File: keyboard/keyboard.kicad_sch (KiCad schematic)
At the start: 117 parts, among them J1 USB_C_Receptacle_USB2.0_16P, SW1 Keyswitch, SW10 Keyswitch, SW11 Keyswitch, SW12 Keyswitch, SW13 Keyswitch, SW14 Keyswitch, SW15 Keyswitch, SW16 Keyswitch, SW17 Keyswitch, SW18 Keyswitch, SW19 Keyswitch, SW2 Keyswitch, SW20 Keyswitch, SW21 Keyswitch, SW22 Keyswitch, SW23 Keyswitch, SW24 Keyswitch, SW25 Keyswitch, SW26 Keyswitch, SW27 Keyswitch, SW29 Keyswitch, SW3 Keyswitch, SW30 Keyswitch, SW31 Keyswitch, SW32 Keyswitch, SW33 Keyswitch, SW34 Keyswitch, SW35 Keyswitch, SW36 Keyswitch, SW37 Keyswitch, SW38 Keyswitch, SW39 Keyswitch, SW4 Keyswitch, SW40 Keyswitch, SW41 Keyswitch, SW42 Keyswitch, SW43 Keyswitch, SW44 Keyswitch, SW45 Keyswitch, SW46 Keyswitch, SW47 Keyswitch, SW48 Keyswitch, SW49 SW_SPDT, SW5 Keyswitch, SW50 SW_Push, SW6 Keyswitch, SW7 Keyswitch, SW8 Keyswitch, SW9 Keyswitch, U1 USBLC6-2P6, U2 STM32F072CBU6, U3 AP2112K-3.3

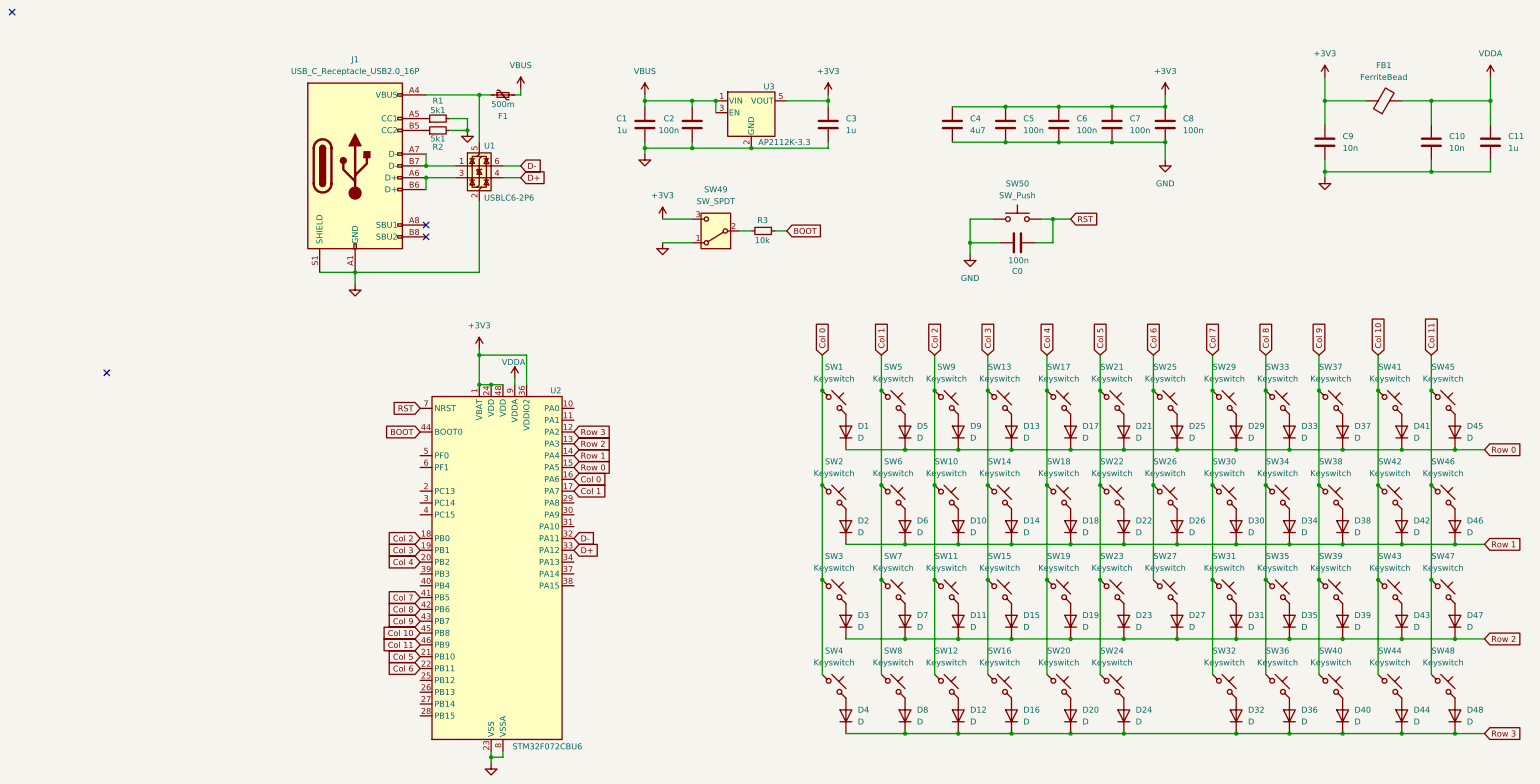
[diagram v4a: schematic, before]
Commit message: feat(keyboard): changed from QFP48 to LQFP48
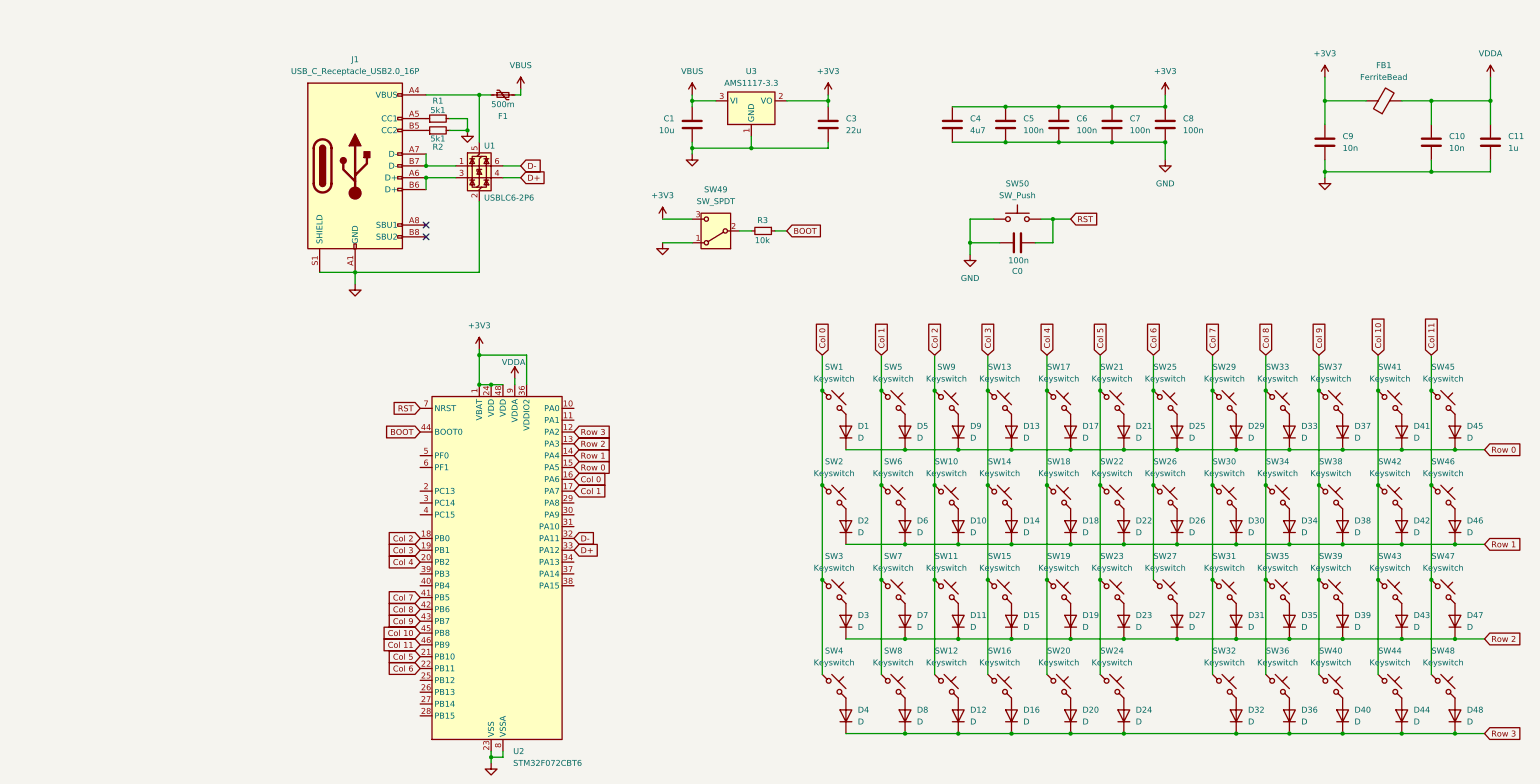
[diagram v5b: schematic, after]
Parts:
- removed C2: 100n, Capacitor_SMD:C_0603_1608Metric, symbol Device:C
- removed U2: STM32F072CBU6, Package_DFN_QFN:QFN-48-1EP_7x7mm_P0.5mm_EP5.6x5.6mm, symbol MCU_ST_STM32F0:STM32F072CBUx
- removed U3: AP2112K-3.3, Package_TO_SOT_SMD:SOT-23-5, symbol Regulator_Linear:AP2112K-3.3
- added U2: STM32F072CBT6, Package_QFP:LQFP-48_7x7mm_P0.5mm, symbol MCU_ST_STM32F0:STM32F072CBTx
- added U3: AMS1117-3.3, Package_TO_SOT_SMD:SOT-223-3_TabPin2, symbol Regulator_Linear:AMS1117-3.3
- C0, C5, C6, C7, C8: LCSC C2909627 -> C14663
- C1: value 1u -> 10u; LCSC C2691405 -> C19702
- C10, C9: LCSC C185599 -> C57112
- C11: LCSC C2691405 -> C15849
- C3: value 1u -> 22u; LCSC C2691405 -> C59461
- C4: LCSC C2918512 -> C19666
- D1, D10, D11, D12, D13, D14, D15, D16, D17, D18, D19, D2, D20, D21, D22, D23, D24, D25, D26, D27, D29, D3, D30, D31, D32, D33, D34, D35, D36, D37, D38, D39, D4, D40, D41, D42, D43, D44, D45, D46, D47, D48, D5, D6, D7, D8, D9: LCSC C402213 -> C81598
- F1: LCSC C3760867 -> C7472536
- FB1: LCSC C491555 -> C1002
- J1: LCSC C319148 -> C2686968
- R1, R2: LCSC C543856 -> C23186
- R3: LCSC C328335 -> C25804
- SW50: LCSC C202424 -> C127478
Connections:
- net +3V3: now also U2.1 (VBAT), U2.24 (VDD), U2.36 (VDDIO2), U2.48 (VDD), U3.2 (VO)
- net BOOT: now also U2.44 (BOOT0)
- net Col 0: now also U2.16 (PA6)
- net Col 1: now also U2.17 (PA7)
- net Col 10: now also U2.45 (PB8)
- net Col 11: now also U2.46 (PB9)
- net Col 2: now also U2.18 (PB0)
- net Col 3: now also U2.19 (PB1)
- net Col 4: now also U2.20 (PB2)
- net Col 5: now also U2.21 (PB10)
- net Col 6: now also U2.22 (PB11)
- net Col 7: now also U2.41 (PB5)
- net Col 8: now also U2.42 (PB6)
- net Col 9: now also U2.43 (PB7)
- net D+: now also U2.33 (PA12)
- net D-: now also U2.32 (PA11)
- net GND: now also U2.23 (VSS), U2.35 (VSS), U2.47 (VSS), U2.8 (VSSA), U3.1 (GND)
- net RST: now also U2.7 (NRST)
- net Row 0: now also U2.15 (PA5)
- net Row 1: now also U2.14 (PA4)
- net Row 2: now also U2.13 (PA3)
- net Row 3: now also U2.12 (PA2)
- net VBUS: now also U3.3 (VI)
- net VDDA: now also U2.9 (VDDA)
- no-connect marks 4 -> 2
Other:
- moved on the sheet: C1
